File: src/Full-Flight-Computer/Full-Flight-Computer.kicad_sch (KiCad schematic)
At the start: 36 parts, among them J1 Jumper_NO, P1 1984659, P3 0530470610, P5 B2B-PH-K-SLFSN_JST, U1 STM32H750VBTx, U3 AP7370-33Y-13, Y1 ECS-240-18-33-JGN-TR

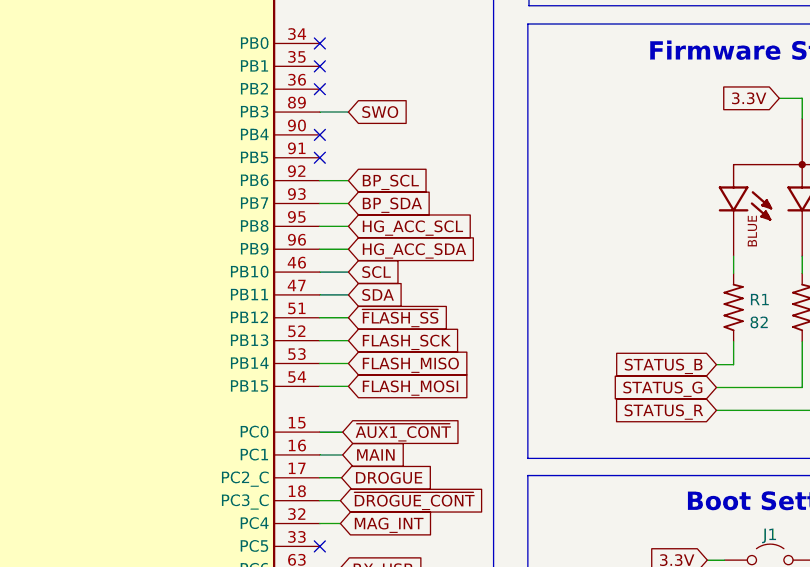
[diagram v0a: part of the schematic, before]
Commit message: add IMU prefix to IMU SDA and SCL labels
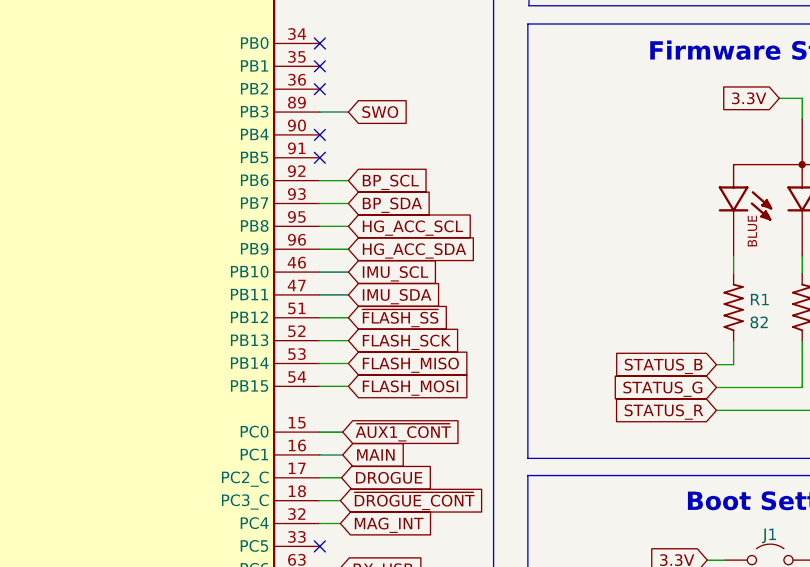
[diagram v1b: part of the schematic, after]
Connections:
- net SCL renamed IMU_SCL
- net SDA renamed IMU_SDA
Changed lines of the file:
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@@
     )
   )
-  (global_label "SDA" (shape input) (at 95.631 121.158 0) (fields_autoplaced)
+  (global_label "IMU_SDA" (shape input) (at 95.631 121.158 0) (fields_autoplaced)
     (effects (font (size 1.27 1.27)) (justify left))
-    (property "Intersheetrefs" "${INTERSHEET_REFS}" (at 101.5233 121.0786 0)
+    (property "Intersheetrefs" "${INTERSHEET_REFS}" (at 105.805 121.158 0)
       (effects (font (size 1.27 1.27)) (justify left) hide)
     )
@@
     )
   )
-  (global_label "SCL" (shape input) (at 95.631 118.618 0) (fields_autoplaced)
+  (global_label "IMU_SCL" (shape input) (at 95.631 118.618 0) (fields_autoplaced)
     (effects (font (size 1.27 1.27)) (justify left))
-    (property "Intersheetrefs" "${INTERSHEET_REFS}" (at 101.4628 118.5386 0)
+    (property "Intersheetrefs" "${INTERSHEET_REFS}" (at 105.7445 118.618 0)
       (effects (font (size 1.27 1.27)) (justify left) hide)
     )
